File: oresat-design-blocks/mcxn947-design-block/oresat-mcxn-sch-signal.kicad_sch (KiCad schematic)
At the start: 31 parts, among them J10 Conn_02x20_Odd_Even, J3 CAN, J4 TERM, J5 10pin ARM SWD, J6 FTDI-UART-6PIN, J9 Conn_02x20_Odd_Even, SW1 RESET, SW2 ISP(BOOT), U1 MCXN947VKLT, U2 TCAN330, Y1 24 MHz, Y2 32.768 KHz

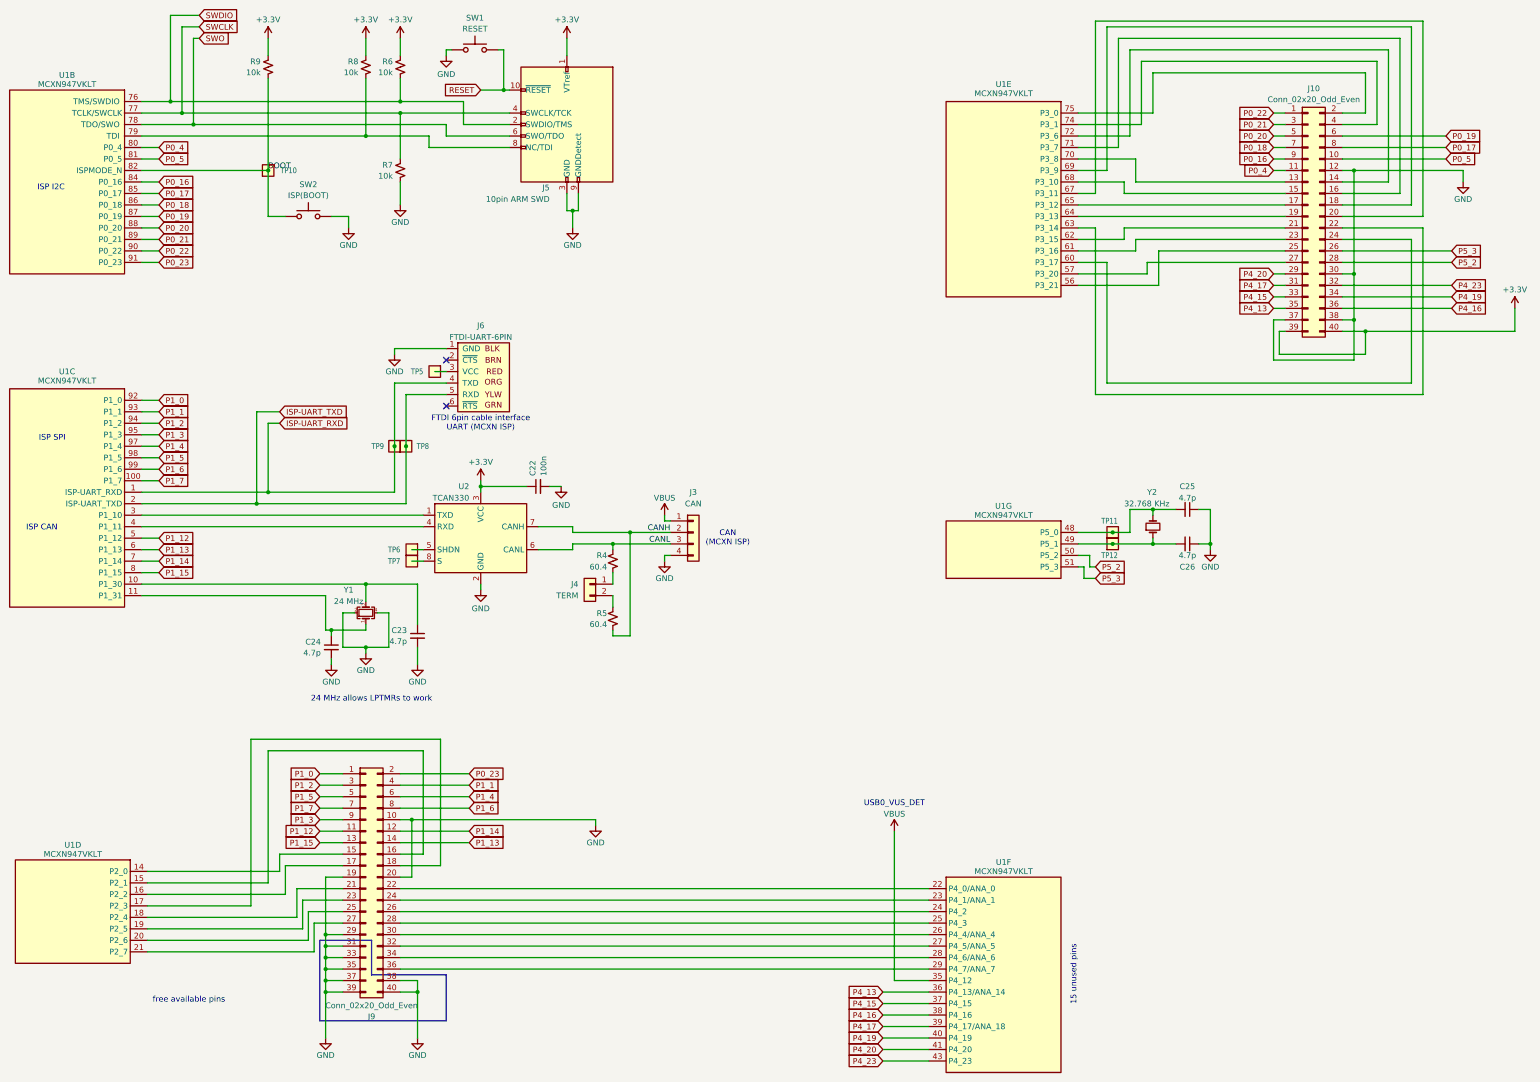
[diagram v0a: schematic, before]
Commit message: Fixed MCXN center pad paste, re-arranged MCXN power pins, and fixed breakout board to hopefully not short.
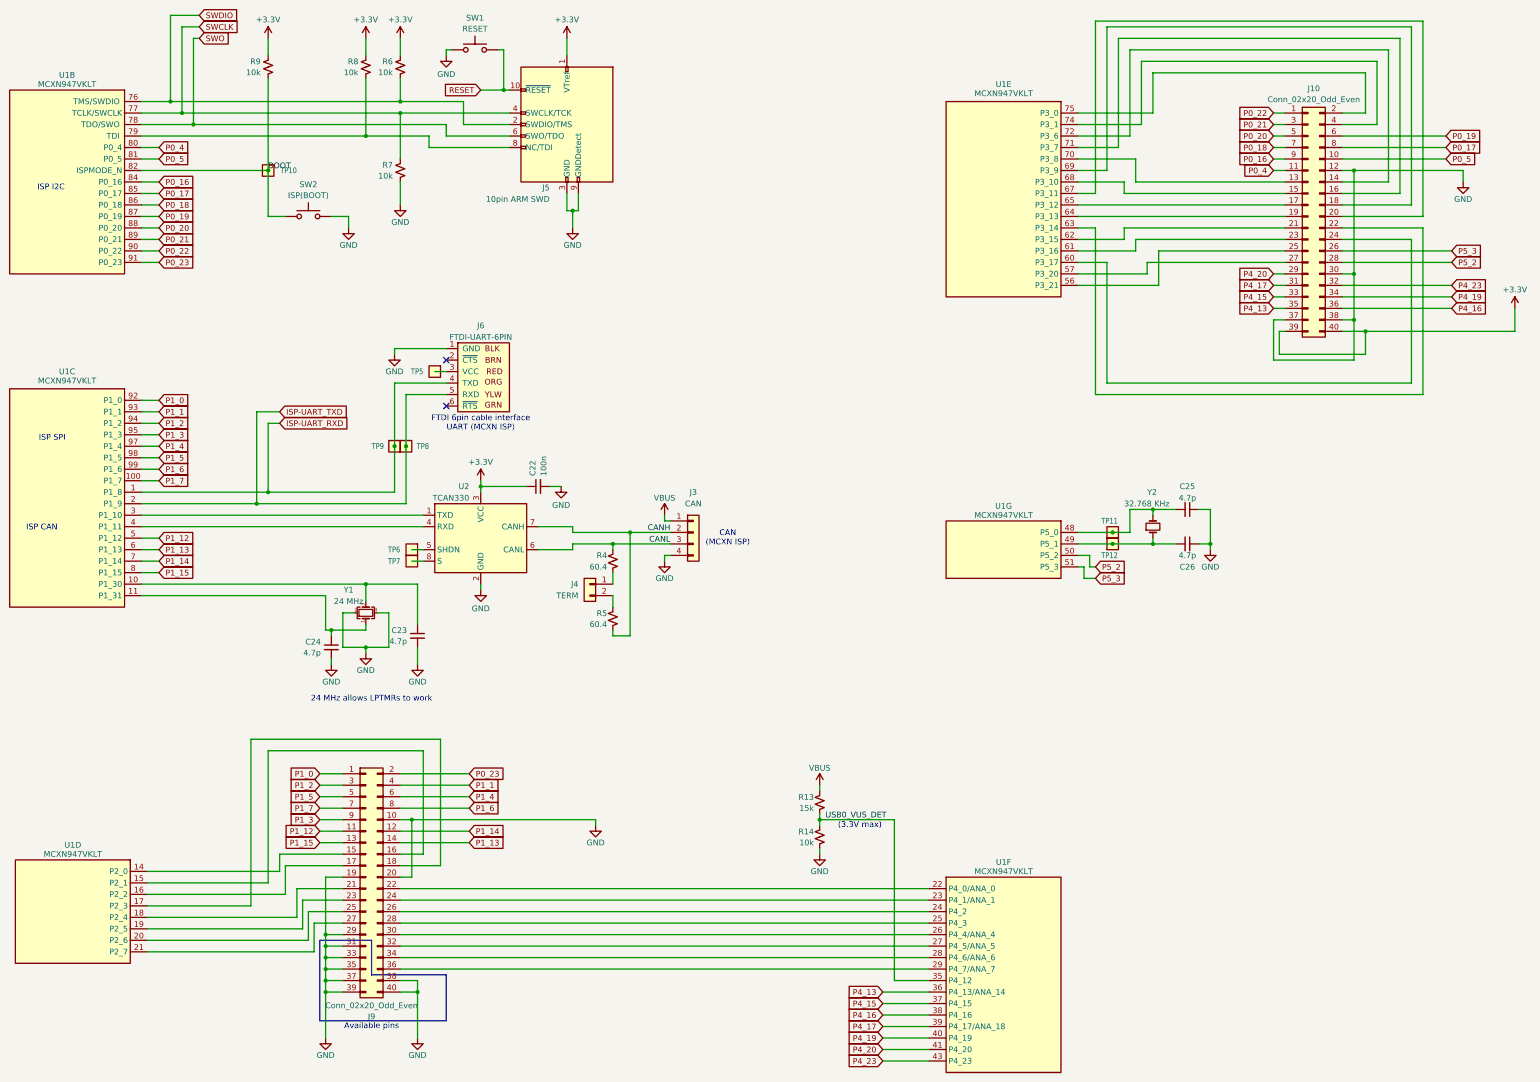
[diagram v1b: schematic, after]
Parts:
- added R13: 15k, oresat-passives:0603-C-NOSILK, symbol Device:R_Small_US
- added R14: 10k, oresat-passives:0603-C-NOSILK, symbol Device:R_Small_US
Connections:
- net GND: now also R14.1
- net VBUS: now also R13.2; no longer U1.35 (P4_12)
- new net USB0_VUS_DET: R13.1, R14.2, U1.35 (P4_12)
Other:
- note added: "(3.3V max)"
- note added: "Available pins"
- note removed: "15 unused pins"
- note removed: "USB0_VUS_DET"
- note removed: "free available pins"

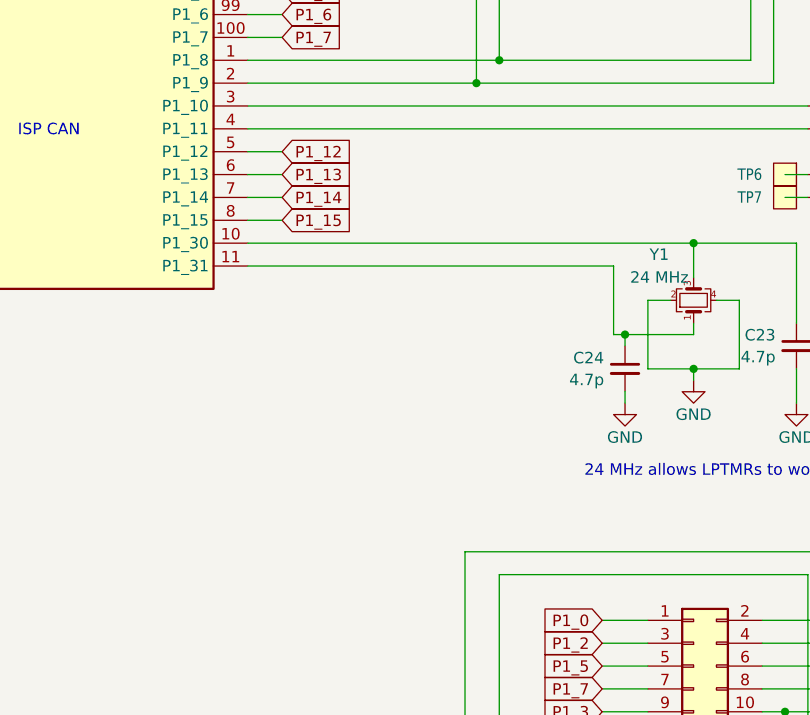
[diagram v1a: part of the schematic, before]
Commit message: Updated BOM with distributor part numbers, lots of double checking. Now truly version 1.1
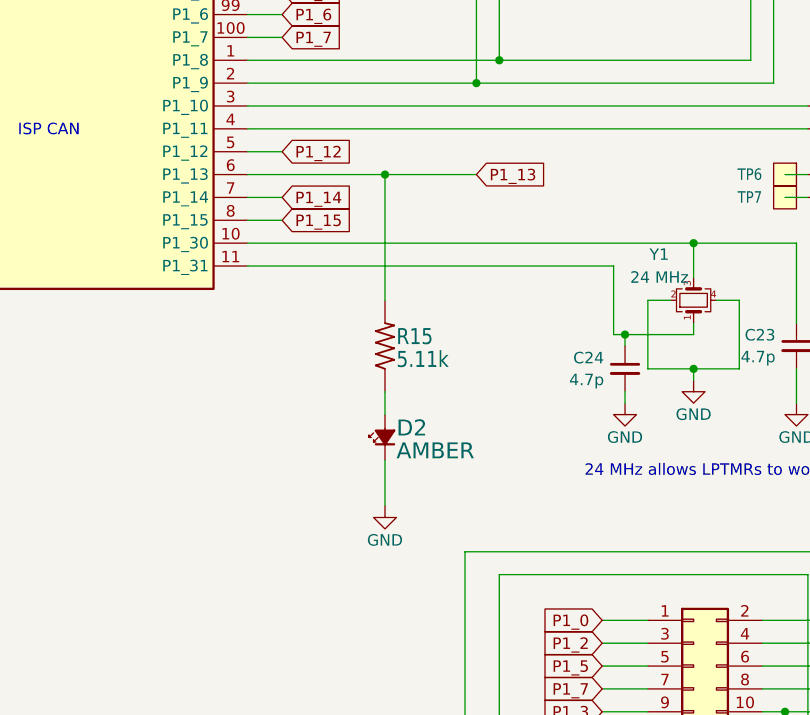
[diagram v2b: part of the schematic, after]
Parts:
- added D2: AMBER, LED_SMD:LED_0603_1608Metric, symbol Device:LED_Small_Filled
- added R15: 5.11k, oresat-passives:0603-C-NOSILK, symbol oresat-passives:R-US
- C22: DIS (none) -> DigiKey; DPN (none) -> 587-3472-1-ND; MFR Murata Electronics -> Taiyo Yuden; MPN GRM188R72A104KA35D -> TMK107BJ104KAHT
- C23, C24, C25, C26: DIS (none) -> DigiKey; DPN (none) -> 490-GRM1885C1H4R7WA01DCT-ND; MFR Murata Electronics -> Murata
- J10, J9: DIS (none) -> DigiKey; DPN (none) -> 2057-PH2-20-UA-ND
- J3: DIS (none) -> DigiKey; DPN (none) -> 2057-PH1-04-UA-ND
- J4: DIS (none) -> DigiKey; DPN (none) -> 2057-PH1-02-UA-ND
- J5: DIS (none) -> DigiKey; DPN (none) -> 2073-BD120-10-A-0305-0229-L-BCT-ND
- J6: DIS (none) -> DigiKey; DPN (none) -> 2057-PH1-06-UA-ND
- R13, R4, R5: DIS (none) -> DigiKey; DPN (none) -> RMCF0603FT60R4CT-ND
- R14: DIS (none) -> DigiKey; DPN (none) -> RMCF0603FT10K0CT-ND; MPN RMCF0603FT60R4 -> RMCF0603FT10K0
- R6, R7, R8, R9: DIS (none) -> DigiKey; DPN (none) -> RMCF0603FT10K0CT-ND
- SW1, SW2: DIS (none) -> DigiKey; DPN (none) -> SW400-ND
- U1: DIS (none) -> Mouser; DPN (none) -> 771-MCXN947VKLT
- U2: DIS (none) -> DigiKey; DPN (none) -> 296-46215-1-ND
- Y1: DIS (none) -> DIgiKey; DPN (none) -> 1923-830108212309CT-ND
- Y2: DIS (none) -> DIgiKey; DPN (none) -> 732-830009678CT-ND
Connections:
- net GND: now also D2.1 (K)
- net P1_13: now also R15.2
- new net: D2.2 (A), R15.1
